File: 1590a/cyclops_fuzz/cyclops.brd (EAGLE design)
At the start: 33 x 52.1 mm, 44 parts, among them IC1 4558, IC2 741

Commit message: updates to cerberus and cyclops
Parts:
- removed D6, D7: 1N914, diodes:DO35-2
- removed IC2: 741, integrated circuits:DIL08
- removed PAD1, PAD2, PAD5: PADSQR, supply pins:SQUARE
- removed PAD3, PAD4: PADRND, supply pins:ROUND
- removed R12: 560k, resistors:R0207/2V
- removed R13: 47R, resistors:R0207/2V
- removed R14: 8k2, resistors:R0207/2V
- removed R15: 470k, resistors:R0207/2V
- removed R16, R17: 47k, resistors:R0207/2V
- removed R18: 100k, resistors:R0207/2V
- removed SUSTAIN: 10kB, potentiometers:2262_TRIM
- added 9V: DC_MONO, jacks:DC
- added C11: 100n, capacitors-film:050X030_025_2
- added GAIN: 100kA, potentiometers:2262_TRIM
- added GND: PADRND, supply pins:ROUND
- added IN, OUT: PADSQR, supply pins:SQUARE
- added U$1: (no value), logos:RT150
- C1: value 150nF -> 47n; device capacitors-film:BOX_SMALL -> capacitors-film:050X030_025_2
- C10: value 1uF -> 150p; device capacitors-film:BOX_MED -> capacitors-film:050X030_025_2
- C3: value 1uF -> 220p; device capacitors-film:BOX_MED -> capacitors-film:050X030_025_2
- C4: value 10nF -> 100n; device capacitors-film:BOX_SMALL -> capacitors-film:050X030_025_2
- C5: value 4.7nF -> 100n; device capacitors-film:BOX_SMALL -> capacitors-film:050X030_025_2
- C6: value .22uF -> 150p; device capacitors-film:BOX_SMALL -> capacitors-film:050X030_025_2
- C7: value 10uF -> 100n; device capacitors-elec:050_020_1 -> capacitors-film:050X030_025_2
- C8: value 1uF -> 150p; device capacitors-elec:050_020_1 -> capacitors-film:050X030_025_2
- C9: value 150pF -> 100n; device capacitors-film:BOX_SMALL -> capacitors-film:050X030_025_2
- D1: value 1N5817 -> (none)
- D2, D3, D4: value 1N914 -> (none); device diodes:DO35-2 -> diodes:DO41-2
- D5: value 1N914 -> 1N5417; device diodes:DO35-2 -> diodes:DO41-3
- IC1: value 4558 -> CD4049; device integrated circuits:DIL08 -> integrated circuits:DIL16
- R1, R9: value 1M -> 100k
- R10: value 820k -> 330k
- R11: value 62k -> 1M
- R2: value 56k -> 100k
- R3: value 47R -> 1M
- R4: value 330k -> 1k
- R5: value 220k -> 33k
- R6: value 220k -> 1M
- R7: value 10k -> 33k
- R8: value 47k -> 1M
- moved D1 46.8 mm to (25.4, 4.45), turned to 90 degrees
- moved R3 35.3 mm to (4.45, 12.7)
- moved D2 32.0 mm to (27.9, 4.45), turned to 270 degrees
- moved C6 31.1 mm to (30.5, 4.45)
- moved C8 30.4 mm to (30.5, 17.1), turned to 270 degrees
- moved C9 28.4 mm to (26.7, 22.2)
- moved R1 26.7 mm to (13.3, 31.8)
- moved C10 23.8 mm to (30.5, 27.3), turned to 90 degrees
- moved R6 23.8 mm to (22.9, 4.45)
- moved D3 23.6 mm to (25.4, 17.1), turned to 90 degrees
- moved R10 22.9 mm to (27.9, 27.3)
- moved R11 19.9 mm to (4.45, 5.08), turned to 0 degrees
- moved C2 19.1 mm to (4.45, 22.9), turned to 270 degrees
- moved R7 19.1 mm to (26.7, 12.1), turned to 0 degrees
- moved R4 19.0 mm to (4.45, 27.3), turned to 0 degrees
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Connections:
- removed net +9V: D1.A, PAD1.1
- removed net N$19: D5.A, D7.C
- removed net N$20: D3.A, D5.C
- removed net VA: C2.+, IC1.8, IC2.7, R10.2, R3.2, R6.2
- removed net VB: C3.1, IC1.5, R5.2, R6.1
- removed net VC: C6.1, IC2.3, R10.1, R9.2
- new net N$15: GAIN.1, R4.2
- net GND: now also 9V.S, GND.1, IC1.3, IC1.5, IC1.8, R11.1, R4.1; no longer C3.2, C4.2, C6.2, C7.-, IC1.4, IC2.4, PAD3.1, PAD4.1, R1.1, R17.1, R18.1, R5.1, R9.1
- net IN: now also C1.2, IN.1, R11.2; no longer C1.1, PAD2.1, R1.2
- net N$1: now also C3.1, C4.2, IC1.6, R3.2; no longer C1.2, R2.1
- net N$10: now also C4.1, GAIN.3; no longer C7.+, R11.1, R13.1
- net N$11: now also C8.1, C9.2, D3.A, D4.C, IC1.12, R8.2; no longer R13.2, SUSTAIN.1
- net N$12: now also C9.1, R9.1; no longer D1.C, R3.1
- net N$13: now also C10.2, IC1.14, R10.1, R9.2; no longer C8.-, SUSTAIN.2
- net N$14: now also C10.1, C11.2, IC1.15, R10.2; no longer C8.+, R14.1
- net N$16: now also C11.1, VOLUME.3; no longer C9.1, D2.A, D3.C, IC2.2, R14.2, R15.1
- net N$17: now also 9V.T, D5.A; no longer D2.C, D4.A
- net N$18: now also C2.+, IC1.1, R1.2; no longer D4.C, D6.A
- net N$2: now also C5.2, GAIN.2; no longer C10.2, R16.1
- net N$21: now also D5.C, R1.1; no longer C10.1, C9.2, D6.C, D7.A, IC2.6, R15.2
- net N$3: now also C3.2, IC1.7, R2.2, R3.1; no longer R16.2, R17.2, VOLUME.3
- net N$4: now also C1.1, R2.1; no longer IC1.6, R2.2, R4.1
- net N$5: now also C5.1, R5.1; no longer IC1.7, R4.2, R7.1
- net N$6: now also C6.2, D1.C, D2.A, IC1.9, R5.2, R6.1; no longer C5.1, R7.2, R8.1
- net N$7: now also C6.1, C7.2, D1.A, D2.C, IC1.10, R6.2; no longer C4.1, IC1.3, R8.2
- net N$8: now also C7.1, R7.1; no longer C5.2, IC1.1, R12.2, SUSTAIN.3
- net N$9: now also C8.2, D3.C, D4.A, IC1.11, R7.2, R8.1; no longer IC1.2, R11.2, R12.1
- net OUT: now also OUT.1; no longer PAD5.1, R18.2
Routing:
- net OUT: track 0.00 -> 39.1 mm
- net N$6: track 0.00 -> 38.2 mm
- net N$13: track 0.00 -> 28.8 mm
- net N$11: track 0.00 -> 19.9 mm
- net N$18: track 0.00 -> 18.5 mm
- net N$14: track 0.00 -> 17.7 mm
- net N$9: track 0.00 -> 17.3 mm
- net N$10: track 0.00 -> 16.8 mm
- net N$7: track 0.00 -> 16.7 mm
- net N$3: track 0.00 -> 12.6 mm
- net IN: track 0.00 -> 10.1 mm
- net N$1: track 0.00 -> 9.04 mm
- net N$2: track 0.00 -> 6.88 mm
- net N$5: track 0.00 -> 6.13 mm
- net N$15: track 0.00 -> 5.72 mm
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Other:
- board size 33 x 52.1 mm -> 33 x 36.8 mm
- board text added: "(c)2016 burr settles"
- board text added: "CYCLOPS FUZZ"

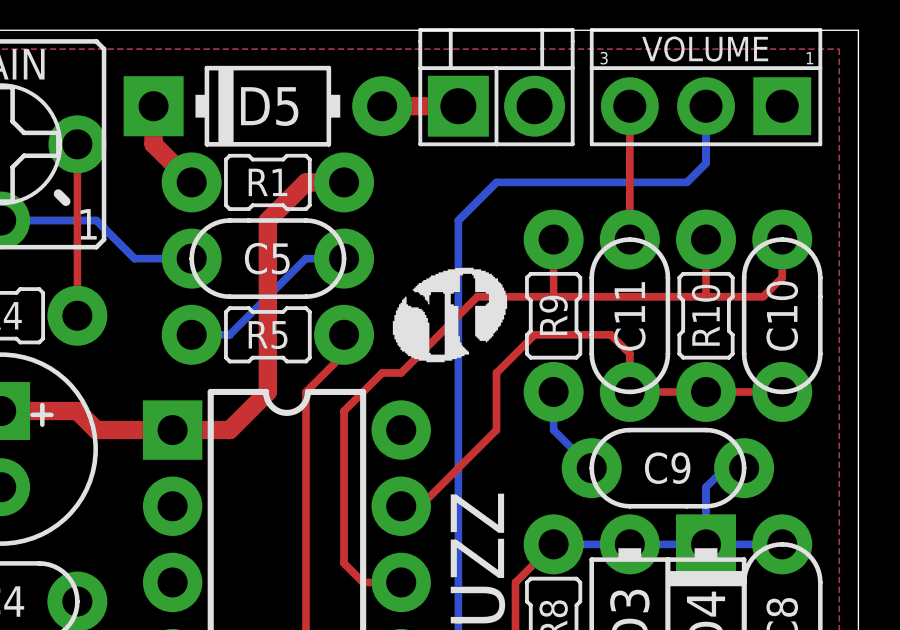
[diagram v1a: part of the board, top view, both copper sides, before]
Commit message: convert bitmap logos to polygons
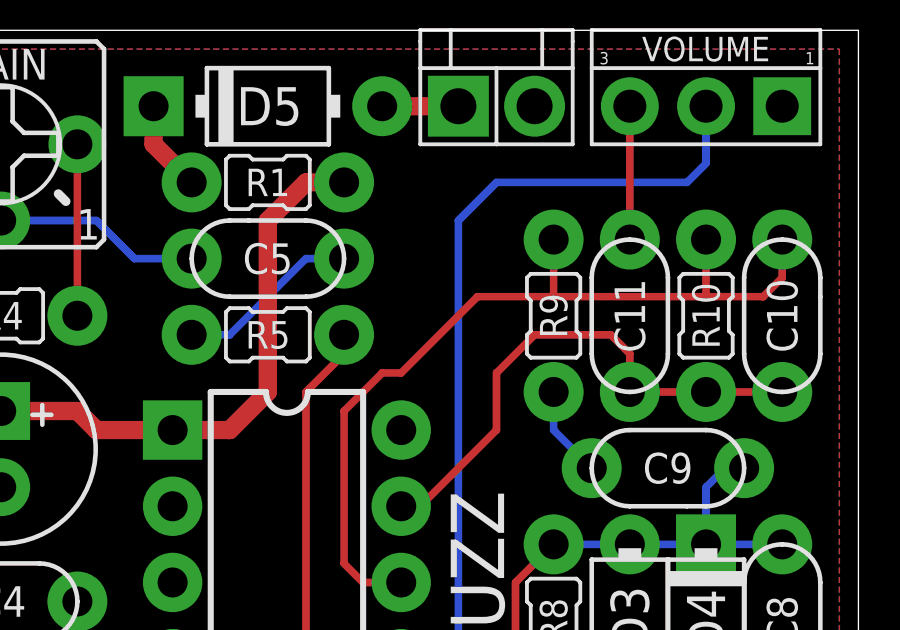
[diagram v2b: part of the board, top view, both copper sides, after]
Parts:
- U$1: device logos:RT150 -> logos:RT0150
- moved U$1 3.05 mm to (19.7, 27.9), turned to 90 degrees
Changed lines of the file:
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@@
 <element name="GND" library="supply pins" package="ROUND" value="PADRND" x="15.875" y="2.54"/>
 <element name="D5" library="diodes" package="DO41-3" value="1N5417" x="13.335" y="34.29"/>
-<element name="U$1" library="logos" package="RT150" value="" x="17.526" y="25.781"/>
+<element name="U$1" library="logos" package="RT0150" value="" x="19.685" y="27.94" rot="R90"/>
 </elements>
 <signals>
